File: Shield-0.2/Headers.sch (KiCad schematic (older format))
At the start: 20 parts, among them J1 EXPANSION, J10 E0 COOL, J11 E0 TEMP, J12 E1 H&T, J13 FAN_0, J14 E0 MOT/STOP, J15 E0 MOT/STOP, J19 E0 HEAT, J2 PWR, J24 PWR, J28 Probe, J4 PWR, J5 E2 H&T, J6 SPADE1, J7 SPADE1, J8 E2 MOT/STOP, J9 E1 MOT/STOP, K1 E0 FAN, P1 STEP, P2 E0 H&T

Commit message: Shield fan header wrong-way-round mistake fixed.
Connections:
- wire segments 281 -> 280

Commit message: Shield - big cap between power connections moved.  Parallel conn for Fan0 added.
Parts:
- removed K1: E0 FAN, symbol CONN_3
- added J16: CONN2, symbol CONN2
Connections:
- wire segments 280 -> 269
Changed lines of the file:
@@
 LIBS:FE
 LIBS:Shield-cache
-EELAYER 27 0
+EELAYER 24 0
 EELAYER END
 $Descr A3 16535 11693
@@
 $EndComp
 $Comp
-L CONN_3 K1
-U 1 1 5465FB61
-P 15150 1450
-F 0 "K1" V 15100 1450 50  0000 C CNN
-F 1 "E0 FAN" V 15200 1450 40  0000 C CNN
-F 2 "" H 15150 1450 60  0001 C CNN
-F 3 "" H 15150 1450 60  0001 C CNN
-	1    15150 1450
-	1    0    0    -1
-$EndComp
-$Comp
 L CONN2 J10
 U 1 1 5465FB2E
@@
 +3.3V
 $Comp
-L GND #PWR016
+L GND #PWR22
 U 1 1 545B8A07
 P 7400 3150
-F 0 "#PWR016" H 7400 3150 30  0001 C CNN
+F 0 "#PWR22" H 7400 3150 30  0001 C CNN
 F 1 "GND" H 7400 3080 30  0001 C CNN
 F 2 "" H 7400 3150 60  0001 C CNN
@@
 VSSA
 $Comp
-L GND #PWR017
+L GND #PWR19
 U 1 1 545B85D0
 P 1600 10750
-F 0 "#PWR017" H 1600 10750 30  0001 C CNN
+F 0 "#PWR19" H 1600 10750 30  0001 C CNN
 F 1 "GND" H 1600 10680 30  0001 C CNN
 F 2 "" H 1600 10750 60  0001 C CNN
@@
 V_IN
 $Comp
-L GND #PWR018
+L GND #PWR18
 U 1 1 545B85C6
 P 1600 10350
-F 0 "#PWR018" H 1600 10350 30  0001 C CNN
+F 0 "#PWR18" H 1600 10350 30  0001 C CNN
 F 1 "GND" H 1600 10280 30  0001 C CNN
 F 2 "" H 1600 10350 60  0001 C CNN
@@
 $EndComp
 $Comp
-L GND #PWR019
+L GND #PWR23
 U 1 1 545B7245
 P 12050 5950
-F 0 "#PWR019" H 12050 5950 30  0001 C CNN
+F 0 "#PWR23" H 12050 5950 30  0001 C CNN
 F 1 "GND" H 12050 5880 30  0001 C CNN
 F 2 "" H 12050 5950 60  0001 C CNN
@@
 Text GLabel 12850 1350 0    60   Output ~ 0
 VSSA
-$Comp
-L GND #PWR020
-U 1 1 545B7132
-P 13150 1600
-F 0 "#PWR020" H 13150 1600 30  0001 C CNN
-F 1 "GND" H 13150 1530 30  0001 C CNN
-F 2 "" H 13150 1600 60  0001 C CNN
-F 3 "" H 13150 1600 60  0001 C CNN
-	1    13150 1600
-	1    0    0    -1
-$EndComp
-$Comp
-L GND #PWR021
-U 1 1 545B7131
-P 13150 1600
-F 0 "#PWR021" H 13150 1600 30  0001 C CNN
-F 1 "GND" H 13150 1530 30  0001 C CNN
-F 2 "" H 13150 1600 60  0001 C CNN
-F 3 "" H 13150 1600 60  0001 C CNN
-	1    13150 1600
-	1    0    0    -1
-$EndComp
-Text GLabel 13550 1450 0    60   Input ~ 0
-V_IN
 Text GLabel 2600 6450 2    60   Input ~ 0
 PROBE-SIG
@@
 PROBE-SIG
 $Comp
-L GND #PWR022
+L GND #PWR17
 U 1 1 53B0339C
 P 1600 9900
-F 0 "#PWR022" H 1600 9900 30  0001 C CNN
+F 0 "#PWR17" H 1600 9900 30  0001 C CNN
 F 1 "GND" H 1600 9830 30  0001 C CNN
 F 2 "" H 1600 9900 60  0001 C CNN
@@
 $EndComp
 $Comp
-L GND #PWR023
+L GND #PWR21
 U 1 1 53B0339B
 P 4300 5800
-F 0 "#PWR023" H 4300 5800 30  0001 C CNN
+F 0 "#PWR21" H 4300 5800 30  0001 C CNN
 F 1 "GND" H 4300 5730 30  0001 C CNN
 F 2 "" H 4300 5800 60  0001 C CNN
@@
 $EndComp
 $Comp
-L GND #PWR024
+L GND #PWR20
 U 1 1 5220B9D2
 P 4100 9900
-F 0 "#PWR024" H 4100 9900 30  0001 C CNN
+F 0 "#PWR20" H 4100 9900 30  0001 C CNN
 F 1 "GND" H 4100 9830 30  0001 C CNN
 F 2 "" H 4100 9900 60  0001 C CNN
@@
 V_IN
 $Comp
-L GND #PWR025
+L GND #PWR16
 U 1 1 5064C39B
 P 1100 950
-F 0 "#PWR025" H 1100 950 30  0001 C CNN
+F 0 "#PWR16" H 1100 950 30  0001 C CNN
 F 1 "GND" H 1100 880 30  0001 C CNN
 F 2 "" H 1100 950 60  0001 C CNN
@@
 	4100 9000 4400 9000
 Wire Wire Line
-	14800 1350 14700 1350
-Wire Wire Line
-	14700 1350 14700 1400
-Wire Wire Line
-	14700 1400 13750 1400
-Wire Wire Line
 	4550 7400 4650 7400
 Wire Wire Line
@@
 	4450 6050 4450 6250
 Wire Wire Line
-	13250 1450 13150 1450
-Wire Wire Line
-	13250 1450 13250 1550
-Wire Wire Line
-	13250 1550 13900 1550
-Wire Wire Line
-	13750 1400 13750 1450
-Wire Wire Line
 	14050 1200 12850 1200
 Wire Wire Line
 	14050 1000 12900 1000
-Wire Wire Line
-	13150 1450 13150 1600
-Wire Wire Line
-	13750 1450 13550 1450
 Connection ~ 13050 1000
 Connection ~ 13050 750
@@
 	14050 1350 14050 1300
 Wire Wire Line
-	13900 1550 13900 1500
-Wire Wire Line
 	14100 4250 14050 4250
 Wire Wire Line
@@
 	4600 7250 4550 7250
 Wire Wire Line
-	13900 1500 14700 1500
-Wire Wire Line
-	14700 1500 14700 1550
-Wire Wire Line
-	14700 1550 14800 1550
-Wire Wire Line
 	4400 9100 4400 8900
 Connection ~ 4400 9000
@@
 	13900 3200 14100 3200
 Wire Wire Line
-	14100 3200 14100 3150
+	14100 3150 14100 3350
 Wire Wire Line
 	14050 1800 12800 1800
@@
 Wire Wire Line
 	13950 1700 13750 1700
+$Comp
+L CONN2 J16
+U 1 1 5491609A
+P 14450 3450
+F 0 "J16" H 14450 3350 40  0000 C CNN
+F 1 "CONN2" V 14600 3500 40  0000 C CNN
+F 2 "" H 14450 3450 60  0000 C CNN
+F 3 "" H 14450 3450 60  0000 C CNN
+	1    14450 3450
+	1    0    0    -1
+$EndComp
+Connection ~ 14100 3200
+Wire Wire Line
+	14100 3450 14000 3450
+Wire Wire Line
+	14000 3450 14000 3000
+Connection ~ 14000 3000
 $EndSCHEMATC

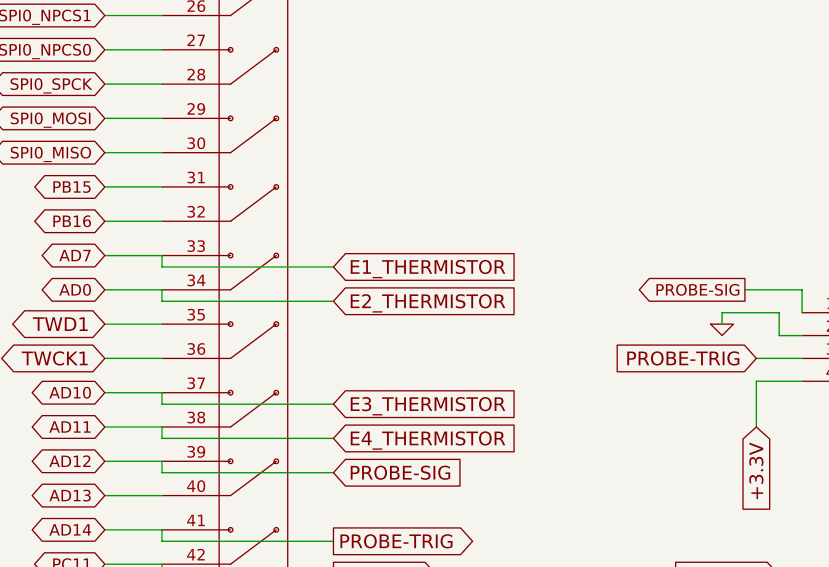
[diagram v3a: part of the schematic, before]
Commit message: Tell-tale LEDs added to Duet 0.7a.
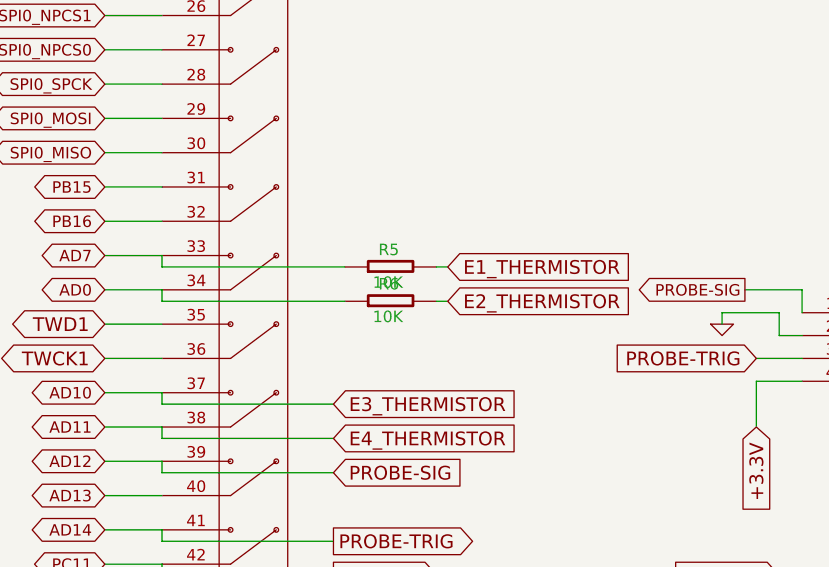
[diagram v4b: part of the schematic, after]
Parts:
- added R5, R6: 10K, symbol R_SMALL
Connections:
- net AD0: now also R6.1; no longer J5.5
- net AD7: now also R5.1; no longer J12.5
- new net E1_THERMISTOR: J12.5, R5.2
- new net E2_THERMISTOR: J5.5, R6.2
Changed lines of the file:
@@
 +3.3V
 $Comp
-L GND #PWR016
+L GND #PWR22
 U 1 1 545B8A07
 P 7400 3150
-F 0 "#PWR016" H 7400 3150 30  0001 C CNN
+F 0 "#PWR22" H 7400 3150 30  0001 C CNN
 F 1 "GND" H 7400 3080 30  0001 C CNN
 F 2 "" H 7400 3150 60  0001 C CNN
@@
 VSSA
 $Comp
-L GND #PWR017
+L GND #PWR19
 U 1 1 545B85D0
 P 1600 10750
-F 0 "#PWR017" H 1600 10750 30  0001 C CNN
+F 0 "#PWR19" H 1600 10750 30  0001 C CNN
 F 1 "GND" H 1600 10680 30  0001 C CNN
 F 2 "" H 1600 10750 60  0001 C CNN
@@
 V_IN
 $Comp
-L GND #PWR018
+L GND #PWR18
 U 1 1 545B85C6
 P 1600 10350
-F 0 "#PWR018" H 1600 10350 30  0001 C CNN
+F 0 "#PWR18" H 1600 10350 30  0001 C CNN
 F 1 "GND" H 1600 10280 30  0001 C CNN
 F 2 "" H 1600 10350 60  0001 C CNN
@@
 $EndComp
 $Comp
-L GND #PWR019
+L GND #PWR23
 U 1 1 545B7245
 P 12050 5950
-F 0 "#PWR019" H 12050 5950 30  0001 C CNN
+F 0 "#PWR23" H 12050 5950 30  0001 C CNN
 F 1 "GND" H 12050 5880 30  0001 C CNN
 F 2 "" H 12050 5950 60  0001 C CNN
@@
 Text GLabel 2600 6150 2    60   Input ~ 0
 E3_THERMISTOR
-Text GLabel 2600 5700 2    60   Input ~ 0
+Text GLabel 3100 5700 2    60   Input ~ 0
 E2_THERMISTOR
-Text GLabel 2600 5550 2    60   Input ~ 0
+Text GLabel 3100 5550 2    60   Input ~ 0
 E1_THERMISTOR
 Text GLabel 2600 4200 2    60   Output ~ 0
@@
 PROBE-SIG
 $Comp
-L GND #PWR020
+L GND #PWR17
 U 1 1 53B0339C
 P 1600 9900
-F 0 "#PWR020" H 1600 9900 30  0001 C CNN
+F 0 "#PWR17" H 1600 9900 30  0001 C CNN
 F 1 "GND" H 1600 9830 30  0001 C CNN
 F 2 "" H 1600 9900 60  0001 C CNN
@@
 $EndComp
 $Comp
-L GND #PWR021
+L GND #PWR21
 U 1 1 53B0339B
 P 4300 5800
-F 0 "#PWR021" H 4300 5800 30  0001 C CNN
+F 0 "#PWR21" H 4300 5800 30  0001 C CNN
 F 1 "GND" H 4300 5730 30  0001 C CNN
 F 2 "" H 4300 5800 60  0001 C CNN
@@
 $EndComp
 $Comp
-L GND #PWR022
+L GND #PWR20
 U 1 1 5220B9D2
 P 4100 9900
-F 0 "#PWR022" H 4100 9900 30  0001 C CNN
+F 0 "#PWR20" H 4100 9900 30  0001 C CNN
 F 1 "GND" H 4100 9830 30  0001 C CNN
 F 2 "" H 4100 9900 60  0001 C CNN
@@
 V_IN
 $Comp
-L GND #PWR023
+L GND #PWR16
 U 1 1 5064C39B
 P 1100 950
-F 0 "#PWR023" H 1100 950 30  0001 C CNN
+F 0 "#PWR16" H 1100 950 30  0001 C CNN
 F 1 "GND" H 1100 880 30  0001 C CNN
 F 2 "" H 1100 950 60  0001 C CNN
@@
 	1850 6300 1850 6250
 Wire Wire Line
-	2600 5700 1850 5700
+	1850 5700 2650 5700
 Wire Wire Line
 	1850 5700 1850 5650
@@
 	1850 5500 1850 5550
 Wire Wire Line
-	1850 5550 2600 5550
+	1850 5550 2650 5550
 Wire Wire Line
 	1850 6100 1850 6150
@@
 	14000 3450 14000 3000
 Connection ~ 14000 3000
+$Comp
+L R_SMALL R5
+U 1 1 5491A983
+P 2850 5550
+F 0 "R5" V 2925 5558 50  0000 C CNN
+F 1 "10K" V 2782 5562 50  0000 C CNN
+F 2 "" H 2850 5550 60  0000 C CNN
+F 3 "" H 2850 5550 60  0000 C CNN
+	1    2850 5550
+	0    -1   -1   0
+$EndComp
+$Comp
+L R_SMALL R6
+U 1 1 5491A992
+P 2850 5700
+F 0 "R6" V 2925 5708 50  0000 C CNN
+F 1 "10K" V 2782 5712 50  0000 C CNN
+F 2 "" H 2850 5700 60  0000 C CNN
+F 3 "" H 2850 5700 60  0000 C CNN
+	1    2850 5700
+	0    -1   -1   0
+$EndComp
+Wire Wire Line
+	3050 5550 3100 5550
+Wire Wire Line
+	3050 5700 3100 5700
 $EndSCHEMATC
